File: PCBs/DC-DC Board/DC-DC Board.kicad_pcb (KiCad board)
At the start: 2 copper layers, 58.4 x 36.8 mm, 38 parts, among them J1 Conn_01x01, J2 Conn_01x01, J3 Conn_01x01, J4 Conn_01x01, J5 Conn_01x02, J6 Conn_01x02, Q1 Q_NMOS_GDS, U1 MurataDC-DC, U2 ACS711, U3 NCP551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

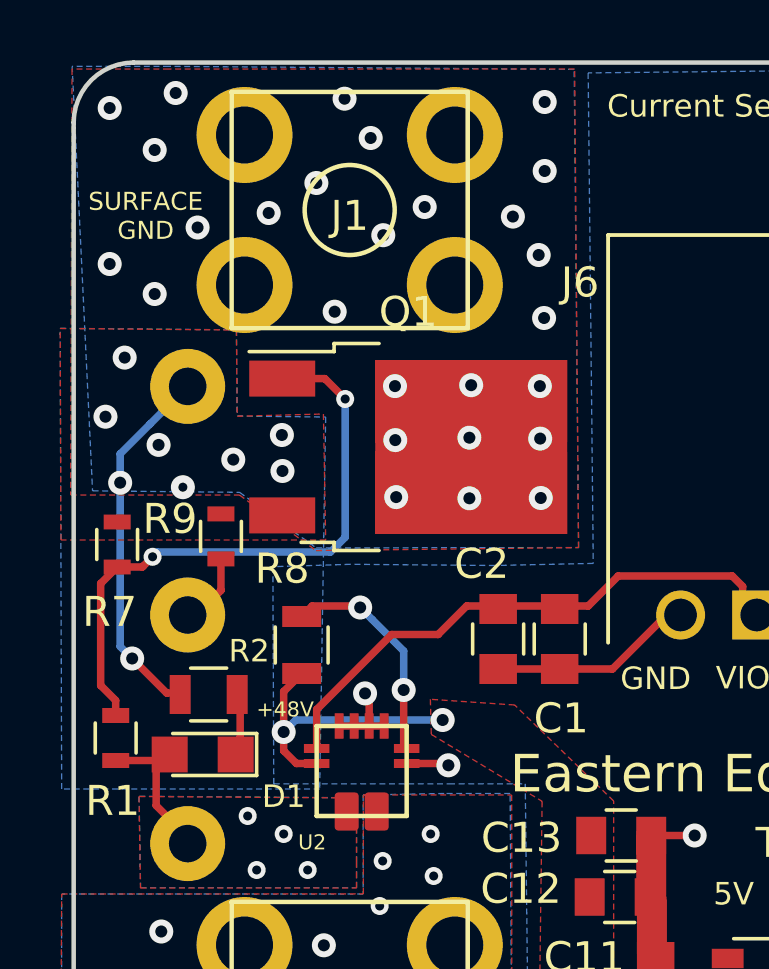
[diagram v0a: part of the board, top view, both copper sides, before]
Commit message: Cleaned up BOM
KiCAD has a built in BOM!! Woohooo!!!
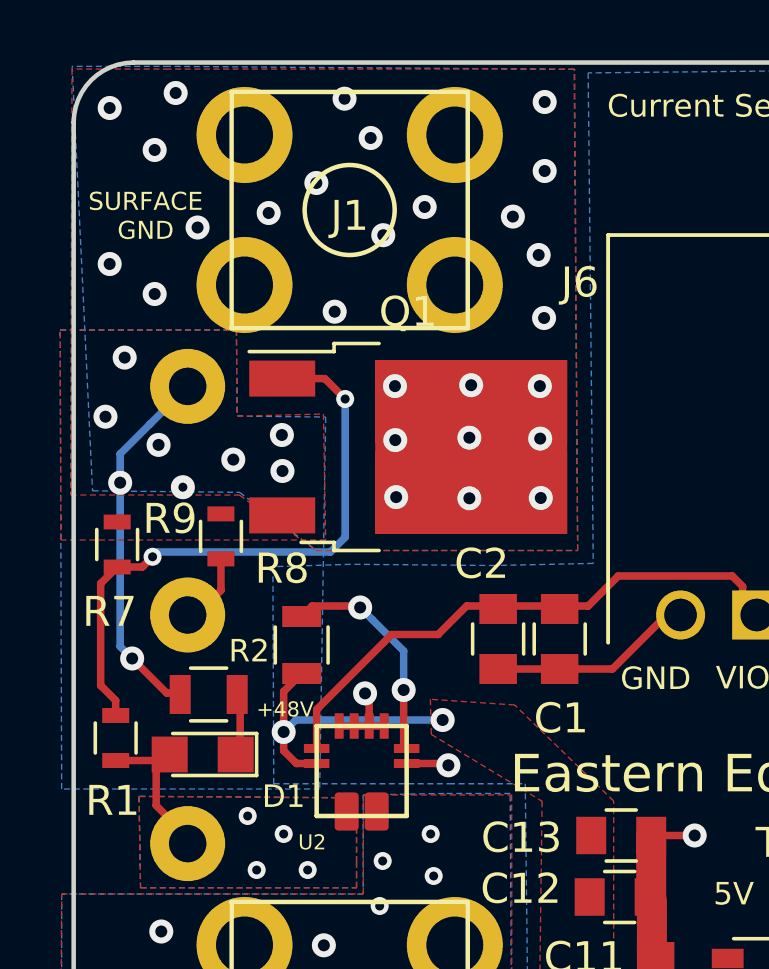
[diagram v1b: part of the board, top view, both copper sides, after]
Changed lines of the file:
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@@
     (polygon
       (pts
-        (xy 78.88 47.852) (xy 87.63 47.752) (xy 87.5 31.8) (xy 73.975633 31.800335) (xy 70.745633 31.800335)
+        (xy 78.88 47.852) (xy 87.6 47.85) (xy 87.5 31.8) (xy 73.975633 31.800335) (xy 70.745633 31.800335)
         (xy 70.7 46) (xy 76.325633 46.000335)
       )
@@
     (polygon
       (pts
-        (xy 79.2 47.5) (xy 70.375 47.5) (xy 70.35 40.45) (xy 76.225 40.5) (xy 76.25 43.375)
+        (xy 79.2 47.5) (xy 70.375 47.5) (xy 70.35 40.5) (xy 76.225 40.5) (xy 76.25 43.375)
         (xy 79.125 43.3)
       )
@@
     (polygon
       (pts
-        (xy 79 55.8) (xy 70.4 55.8) (xy 70.35 40.445) (xy 76.225 40.495) (xy 76.25 43.37)
+        (xy 79 55.8) (xy 70.4 55.8) (xy 70.35 40.5) (xy 76.225 40.495) (xy 76.25 43.37)
         (xy 79.2 43.4)
       )
@@
     (polygon
       (pts
-        (xy 78.884038 47.762868) (xy 87.63 47.752) (xy 87.484038 31.812868) (xy 73.979671 31.711203) (xy 70.749671 31.711203)
+        (xy 78.9 47.85) (xy 87.6 47.85) (xy 87.484038 31.812868) (xy 73.979671 31.711203) (xy 70.749671 31.711203)
         (xy 71.429671 45.861203) (xy 76.329671 45.911203)
       )

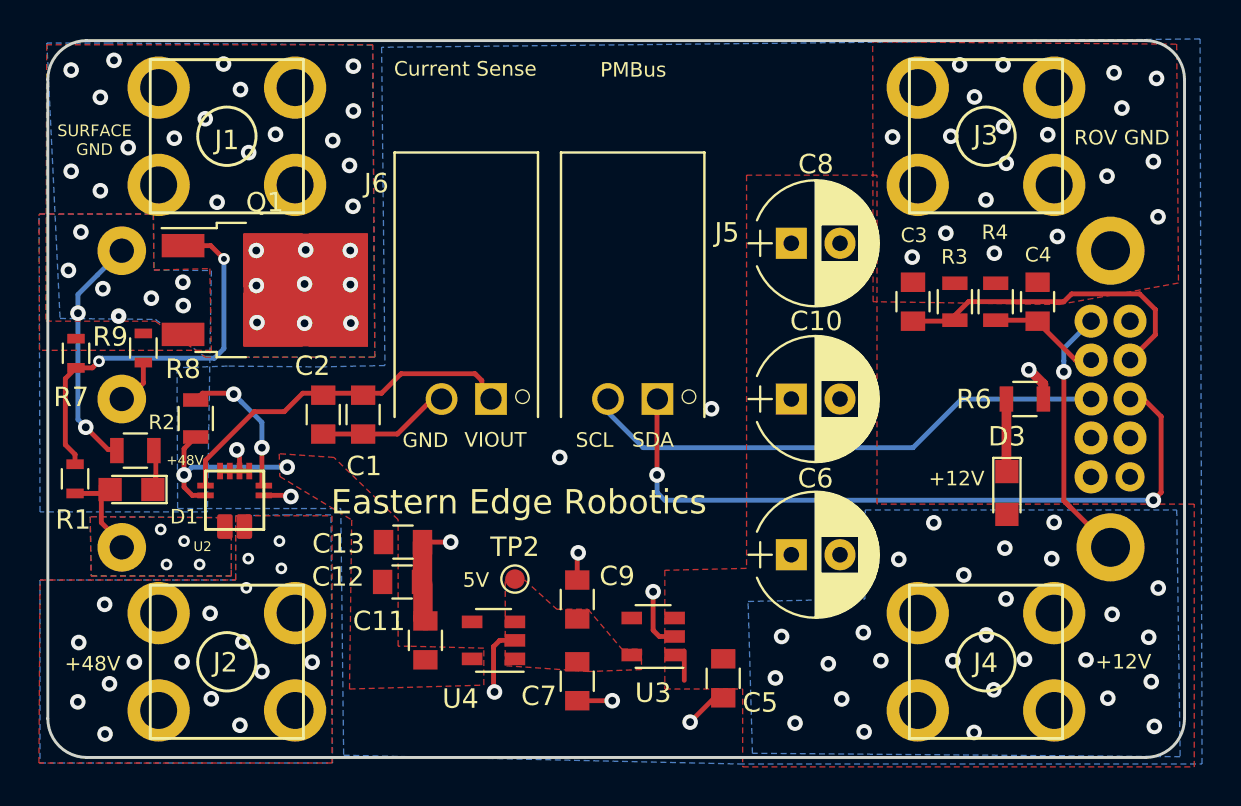
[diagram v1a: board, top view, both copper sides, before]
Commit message: Started DC-DC with Micro
Picked out microcontroller maybe? Still gotta decide if I want to use the 5x5 vs the 7x7.
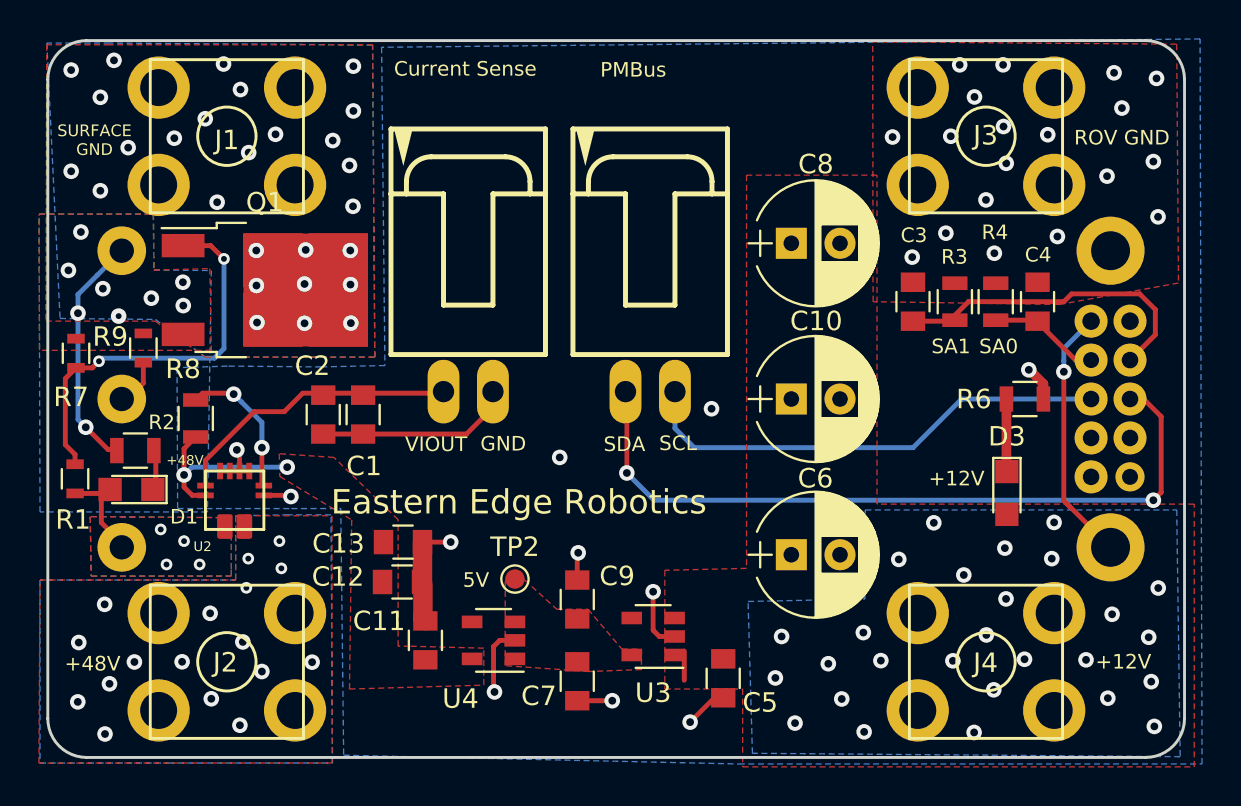
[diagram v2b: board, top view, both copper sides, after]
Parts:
- J5, J6: footprint EER:MOLEX_0705530001 -> EER:70553-02
- R1: value 700k -> 698k
- U1: value MurataDC-DC -> DBQ0135V2
- moved J6 8.09 mm to (92.4, 42.0), turned to 0 degrees
- moved J5 8.01 mm to (101.8, 42.0), turned to 0 degrees
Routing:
- net GND: track 30.4 -> 35.1 mm
- net VIOUT: track 18.4 -> 15.0 mm
- net SCL: track 27.5 -> 24.7 mm
- net SDA: track 37.1 -> 38.3 mm
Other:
- board text added: "SA0"
- board text added: "SA1"

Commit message: DC-DC Mirco Updates
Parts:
- moved J5 3.01 mm to (102.0, 45.0)
- moved J6 3.00 mm to (92.4, 45.0)
- moved C13 0.65 mm to (89.0, 58.0)
- moved C12 0.40 mm to (89.0, 59.8)
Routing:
- net GND: track 35.1 -> 27.0 mm, vias 30 -> 29
- net SDA: track 38.3 -> 34.1 mm, vias 2 -> 1
- net SCL: track 24.7 -> 21.4 mm
- net VIOUT: track 15.0 -> 16.6 mm

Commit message: DC-DC Boards 99%
Both boards are pretty much done. They just need a few double checks and some BOM work has to be done for the Micro Board.
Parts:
- moved J5 3.00 mm to (102.0, 48.0)
- moved J6 3.00 mm to (92.4, 48.0)
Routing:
- net SCL: track 21.4 -> 24.9 mm
- net VIOUT: track 16.6 -> 19.9 mm
- net SDA: track 34.1 -> 36.7 mm
- net GND: track 27.0 -> 28.6 mm, vias 29 -> 30
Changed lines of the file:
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@@
     (thickness 1.6)
     (drawings 26)
-    (tracks 251)
+    (tracks 261)
     (zones 0)
     (modules 38)
@@
   )
   (module EER:70553-02 (layer F.Cu)
-    (at 92.4 45)
+    (at 92.4 48)
     (descr "<b>2.54mm Pitch SL™ Header, Low Profile, Single Row, Right Angle, 3.05mm Pocket, Shrouded, 3 Circuits, 0.38µm Gold (Au) Selective Plating, Tin (Sn) PC Tail Plating</b><p><a href =http://www.molex.com/pdm_docs/sd/705530002_sd.pdf>Datasheet </a>")
     (fp_text reference J6 (at -4.445 5.715 90) (layer F.SilkS) hide
@@
     (tags "test point SMD pad")
     (attr virtual)
-    (fp_text reference TP2 (at 0 -1.65) (layer F.SilkS)
+    (fp_text reference TP2 (at 0.875 -1.25) (layer F.SilkS)
       (effects (font (size 1 1) (thickness 0.15)))
     )
@@
   )
   (module EER:70553-02 (layer F.Cu)
-    (at 102 45)
+    (at 102 48)
     (descr "<b>2.54mm Pitch SL™ Header, Low Profile, Single Row, Right Angle, 3.05mm Pocket, Shrouded, 3 Circuits, 0.38µm Gold (Au) Selective Plating, Tin (Sn) PC Tail Plating</b><p><a href =http://www.molex.com/pdm_docs/sd/705530002_sd.pdf>Datasheet </a>")
     (fp_text reference J5 (at -4.445 5.715 90) (layer F.SilkS) hide
@@
     (effects (font (size 0.75 0.75) (thickness 0.1875)))
   )
-  (gr_text "GND\n" (at 95.95 53.7) (layer F.SilkS)
+  (gr_text "GND\n" (at 95.8 55.625) (layer F.SilkS)
     (effects (font (size 0.75 0.75) (thickness 0.1875)))
   )
@@
     (effects (font (size 0.75 0.75) (thickness 0.1875)))
   )
-  (gr_text "VIOUT\n" (at 88.275 53.75) (layer F.SilkS)
+  (gr_text "VIOUT\n" (at 88.4 55.65) (layer F.SilkS)
     (effects (font (size 0.75 0.75) (thickness 0.1875)))
   )
-  (gr_text "SCL\n" (at 105.525 53.8) (layer F.SilkS)
+  (gr_text "SCL\n" (at 105.525 55.6) (layer F.SilkS)
     (effects (font (size 0.75 0.75) (thickness 0.1875)))
   )
-  (gr_text "SDA\n" (at 98.575 53.7) (layer F.SilkS)
+  (gr_text "SDA\n" (at 98.4 55.6) (layer F.SilkS)
     (effects (font (size 0.75 0.75) (thickness 0.1875)))
   )
@@
     (effects (font (size 0.75 0.75) (thickness 0.125)) (justify mirror))
   )
-  (gr_text "Eastern Edge Robotics" (at 96.05 55.5) (layer F.SilkS)
+  (gr_text "Eastern Edge Robotics" (at 97.05 67) (layer F.SilkS)
     (effects (font (size 1.25 1.25) (thickness 0.3)))
   )
@@
   (gr_line (start 129.2 33.585) (end 129.2 66.415) (layer Edge.Cuts) (width 0.15))
   (gr_line (start 72.8 31.585) (end 127.2 31.585) (layer Edge.Cuts) (width 0.15))
+  (via (at 122 51.725) (size 0.8) (drill 0.4) (layers F.Cu B.Cu) (net 3))
   (via (at 81.1 58.2) (size 0.6) (drill 0.3) (layers F.Cu B.Cu) (net 1))
   (via (at 82.7 57.3) (size 0.6) (drill 0.3) (layers F.Cu B.Cu) (net 1))
@@
   (via (at 83.29 55.01) (size 0.8) (drill 0.4) (layers F.Cu B.Cu) (net 3))
   (via (at 121.2 48.5) (size 0.8) (drill 0.4) (layers F.Cu B.Cu) (net 3))
-  (via (at 103.8 66.6) (size 0.8) (drill 0.4) (layers F.Cu B.Cu) (net 3))
-  (segment (start 105.5 65.35) (end 105.05 65.35) (width 0.25) (layer F.Cu) (net 3))
-  (segment (start 105.05 65.35) (end 103.8 66.6) (width 0.25) (layer F.Cu) (net 3))
   (segment (start 121.975 49.775) (end 121.975 49.725) (width 0.25) (layer F.Cu) (net 3))
   (segment (start 121.225 48.5) (end 121.2 48.5) (width 0.5) (layer F.Cu) (net 3))
@@
   (segment (start 90 59.3) (end 90.05 59.35) (width 1) (layer F.Cu) (net 3))
   (segment (start 90.025 58.175) (end 90 59.3) (width 1) (layer F.Cu) (net 3))
-  (segment (start 89.925 58.225) (end 91.325 58.25) (width 0.25) (layer F.Cu) (net 3))
-  (via (at 91.325 58.25) (size 0.8) (drill 0.4) (layers F.Cu B.Cu) (net 3))
+  (via (at 103.825 65.475) (size 0.8) (drill 0.4) (layers F.Cu B.Cu) (net 3))
+  (segment (start 105.05 65.35) (end 105.5 65.35) (width 0.25) (layer F.Cu) (net 3))
+  (segment (start 103.825 65.475) (end 105.05 65.35) (width 0.25) (layer F.Cu) (net 3))
+  (segment (start 89.925 58.225) (end 91.625 58.775) (width 0.25) (layer F.Cu) (net 3))
+  (via (at 91.625 58.775) (size 0.8) (drill 0.4) (layers F.Cu B.Cu) (net 3))
+  (segment (start 122 50.05) (end 121.95 50) (width 0.25) (layer F.Cu) (net 3))
+  (segment (start 122 51.725) (end 122 50.05) (width 0.25) (layer F.Cu) (net 3))
   (segment (start 74.35 52.6) (end 73.9 52.6) (width 0.25) (layer F.Cu) (net 4))
   (via (at 72.75 51.45) (size 0.8) (drill 0.4) (layers F.Cu B.Cu) (net 4))
@@
   (segment (start 78.9 53.15) (end 81.4 50.65) (width 0.25) (layer F.Cu) (net 5))
   (segment (start 84.95 49.8) (end 87 49.8) (width 0.25) (layer F.Cu) (net 5))
-  (segment (start 91.13 51.80085) (end 91.13 52.62) (width 0.25) (layer F.Cu) (net 5))
   (segment (start 89.12915 49.8) (end 91.13 51.80085) (width 0.25) (layer F.Cu) (net 5))
   (segment (start 87 49.8) (end 89.12915 49.8) (width 0.25) (layer F.Cu) (net 5))
+  (segment (start 91.13 55.62) (end 91.13 52.325) (width 0.25) (layer F.Cu) (net 5))
+  (segment (start 91.13 51.80085) (end 91.13 52.325) (width 0.25) (layer F.Cu) (net 5))
+  (segment (start 91.13 52.325) (end 91.13 52.62) (width 0.25) (layer F.Cu) (net 5))
   (segment (start 117.35 46) (end 117.4 45.95) (width 0.25) (layer F.Cu) (net 6))
   (segment (start 115.25 46) (end 117.35 46) (width 0.25) (layer F.Cu) (net 6))
@@
   (segment (start 126.4 50) (end 127.1 50) (width 0.25) (layer F.Cu) (net 12))
   (segment (start 127.1 50) (end 128 50.9) (width 0.25) (layer F.Cu) (net 12))
-  (segment (start 101.95 55.2) (end 100.55 53.8) (width 0.25) (layer B.Cu) (net 12))
-  (segment (start 127.6 55.2) (end 101.95 55.2) (width 0.25) (layer B.Cu) (net 12))
+  (segment (start 107.3 55.275) (end 127.6 55.2) (width 0.25) (layer B.Cu) (net 12))
+  (segment (start 104.25 58.325) (end 107.3 55.275) (width 0.25) (layer B.Cu) (net 12))
+  (segment (start 101.8 58.325) (end 104.25 58.325) (width 0.25) (layer B.Cu) (net 12))
+  (segment (start 100.73 55.62) (end 100.73 57.255) (width 0.25) (layer B.Cu) (net 12))
+  (segment (start 100.73 57.255) (end 101.8 58.325) (width 0.25) (layer B.Cu) (net 12))
   (segment (start 117.75 50) (end 124.4 50) (width 0.25) (layer B.Cu) (net 13))
   (segment (start 115.25 52.5) (end 117.75 50) (width 0.25) (layer B.Cu) (net 13))
   (segment (start 104.0117 52.5) (end 115.25 52.5) (width 0.25) (layer B.Cu) (net 13))
+  (segment (start 103.27 53.2417) (end 103.27 55.62) (width 0.25) (layer B.Cu) (net 13))
+  (segment (start 104.0117 52.5) (end 103.27 53.2417) (width 0.25) (layer B.Cu) (net 13))
   (segment (start 81.9 54.45) (end 82.175 54.45) (width 0.25) (layer F.Cu) (net 16))
   (via (at 81.8 52.5) (size 0.8) (drill 0.4) (layers F.Cu B.Cu) (net 16))
@@
     (polygon
       (pts
-        (xy 88.07 55.91) (xy 92.8 54.925) (xy 96.4 54.15) (xy 96.425 51.25) (xy 96.539228 30.34296)
-        (xy 97.625 30.675) (xy 97.55 54.725) (xy 94.6 55.45) (xy 88.55 56.65)
+        (xy 89.875 57.45) (xy 95.4 56.8) (xy 96.45 54.175) (xy 96.425 51.25) (xy 96.539228 30.34296)
+        (xy 97.625 30.675) (xy 97.55 54.725) (xy 96.375 57.525) (xy 90.25 58.225)
       )
     )
